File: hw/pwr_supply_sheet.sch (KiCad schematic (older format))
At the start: 16 parts

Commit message: creating hw 3.0.0
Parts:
- added D205: SCHOTTKY_DIODE_V40PW10C, usevolt:SlimDPAK, symbol SCHOTTKY_DIODE_V40PW10C
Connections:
- net VDD: now also D205.3 (CATHODE); no longer D202.P$1 (P)
- new net VIN: D202.P$1 (P), D205.1 (A1), D205.2 (A2)
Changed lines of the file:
@@
 $Descr A4 11693 8268
 encoding utf-8
-Sheet 2 11
+Sheet 2 12
 Title "Power supply"
 Date "2016-08-20"
@@
 Comment4 ""
 $EndDescr
-Text HLabel 1350 3850 0    60   Input ~ 0
+Text HLabel 900  3850 0    60   Input ~ 0
 VIN
 $Comp
@@
 	6850 3600 6850 3850
 $Comp
-L +5V #PWR06
+L +5V #PWR207
 U 1 1 57B831F8
 P 6850 3600
-F 0 "#PWR06" H 6850 3450 50  0001 C CNN
+F 0 "#PWR207" H 6850 3450 50  0001 C CNN
 F 1 "+5V" H 6865 3773 50  0000 C CNN
 F 2 "" H 6850 3600 50  0000 C CNN
@@
 Connection ~ 6850 3750
 $Comp
-L +3V3 #PWR07
+L +3V3 #PWR208
 U 1 1 57B83259
 P 8600 3600
-F 0 "#PWR07" H 8600 3450 50  0001 C CNN
+F 0 "#PWR208" H 8600 3450 50  0001 C CNN
 F 1 "+3V3" H 8615 3773 50  0000 C CNN
 F 2 "" H 8600 3600 50  0000 C CNN
@@
 $EndComp
 Wire Wire Line
-	1350 3850 1700 3850
+	900  3850 1700 3850
 Wire Wire Line
 	3800 3700 4550 3700
@@
 Wire Wire Line
 	8750 3600 8600 3600
-Text HLabel 1350 3450 0    60   Output ~ 0
+Text HLabel 950  5000 0    60   Output ~ 0
 VDD
 Text HLabel 2700 4300 0    60   Input ~ 0
@@
 NoConn ~ 4550 4050
 $Comp
-L VDD #PWR08
+L VDD #PWR205
 U 1 1 57B9C56A
 P 3800 2100
-F 0 "#PWR08" H 3800 1950 50  0001 C CNN
+F 0 "#PWR205" H 3800 1950 50  0001 C CNN
 F 1 "VDD" H 3817 2273 50  0000 C CNN
 F 2 "" H 3800 2100 50  0000 C CNN
@@
 $EndComp
 $Comp
-L PWR_FLAG #FLG09
+L PWR_FLAG #FLG201
 U 1 1 57B9C59C
 P 3800 2300
-F 0 "#FLG09" H 3800 2395 50  0001 C CNN
+F 0 "#FLG201" H 3800 2395 50  0001 C CNN
 F 1 "PWR_FLAG" H 3800 2523 50  0000 C CNN
 F 2 "" H 3800 2300 50  0000 C CNN
@@
 	3800 2300 3800 2100
 $Comp
-L GND #PWR010
+L GND #PWR206
 U 1 1 57B9D351
 P 4300 2350
-F 0 "#PWR010" H 4300 2100 50  0001 C CNN
+F 0 "#PWR206" H 4300 2100 50  0001 C CNN
 F 1 "GND" H 4305 2177 50  0000 C CNN
 F 2 "" H 4300 2350 50  0000 C CNN
@@
 $EndComp
 $Comp
-L PWR_FLAG #FLG011
+L PWR_FLAG #FLG202
 U 1 1 57B9D3A1
 P 4300 2150
-F 0 "#FLG011" H 4300 2245 50  0001 C CNN
+F 0 "#FLG202" H 4300 2245 50  0001 C CNN
 F 1 "PWR_FLAG" H 4300 2374 50  0000 C CNN
 F 2 "" H 4300 2150 50  0000 C CNN
@@
 	4300 2150 4300 2350
 $Comp
-L GND #PWR012
+L GND #PWR204
 U 1 1 57CF1F5E
 P 2800 4500
-F 0 "#PWR012" H 2800 4250 50  0001 C CNN
+F 0 "#PWR204" H 2800 4250 50  0001 C CNN
 F 1 "GND" H 2805 4327 50  0000 C CNN
 F 2 "" H 2800 4500 50  0000 C CNN
@@
 	3800 3850 3800 3700
 Wire Wire Line
-	1350 3450 1500 3450
-Wire Wire Line
-	1500 3450 1500 3850
+	950  5000 1150 5000
 Connection ~ 1500 3850
 Wire Wire Line
@@
 VBAT
 $Comp
-L +BATT #PWR013
+L +BATT #PWR202
 U 1 1 5988E784
 P 2400 1950
-F 0 "#PWR013" H 2400 1800 50  0001 C CNN
+F 0 "#PWR202" H 2400 1800 50  0001 C CNN
 F 1 "+BATT" H 2415 2123 50  0000 C CNN
 F 2 "" H 2400 1950 50  0000 C CNN
@@
 Connection ~ 1550 2700
 $Comp
-L GND #PWR014
+L GND #PWR201
 U 1 1 5988FF98
 P 1550 3150
-F 0 "#PWR014" H 1550 2900 50  0001 C CNN
+F 0 "#PWR201" H 1550 2900 50  0001 C CNN
 F 1 "GND" H 1555 2977 50  0000 C CNN
 F 2 "" H 1550 3150 50  0000 C CNN
@@
 $EndComp
 $Comp
-L GND #PWR015
+L GND #PWR203
 U 1 1 598C262D
 P 2400 2950
-F 0 "#PWR015" H 2400 2700 50  0001 C CNN
+F 0 "#PWR203" H 2400 2700 50  0001 C CNN
 F 1 "GND" H 2405 2777 50  0000 C CNN
 F 2 "" H 2400 2950 50  0000 C CNN
@@
 	2400 2950 2400 2850
 Wire Wire Line
-	2400 2550 2400 2450
+	2400 2450 2400 2550
 Connection ~ 2400 2050
 Wire Wire Line
@@
 Text HLabel 2800 2500 2    60   Output ~ 0
 VBAT_SENSE
+$Comp
+L SCHOTTKY_DIODE_V40PW10C D205
+U 1 1 59C29BB6
+P 1550 5050
+F 0 "D205" H 1550 5397 60  0000 C CNN
+F 1 "SCHOTTKY_DIODE_V40PW10C" H 1550 5291 60  0000 C CNN
+F 2 "usevolt:SlimDPAK" H 1350 4700 60  0001 C CNN
+F 3 "http://www.farnell.com/datasheets/2245239.pdf?_ga=2.16591231.874534928.1505194133-1862443086.1504075057" H 1350 4700 60  0001 C CNN
+F 4 "2535169" H 1900 5650 60  0001 C CNN "1st Source Part Number"
+F 5 "Digikey" H 2000 5750 60  0001 C CNN "2nd Source"
+F 6 "Farnell" H 1800 5550 60  0001 C CNN "1st Source"
+F 7 "V40PW10CHM3/I" H 1700 5450 60  0001 C CNN "Manufacturer Part Number"
+F 8 "V40PW10CHM3/IGICT-ND" H 2100 5850 60  0001 C CNN "2nd Source Part Number"
+F 9 "VISHAY" H 1600 5350 60  0001 C CNN "Manufacturer"
+	1    1550 5050
+	-1   0    0    -1
+$EndComp
+Wire Wire Line
+	1950 5050 2250 5050
+Wire Wire Line
+	2250 5050 2250 4350
+Wire Wire Line
+	2250 4350 1500 4350
+Wire Wire Line
+	1500 4350 1500 3850
+Wire Wire Line
+	1950 4950 2100 4950
+Wire Wire Line
+	2100 4950 2100 5050
+Connection ~ 2100 5050
 $EndSCHEMATC

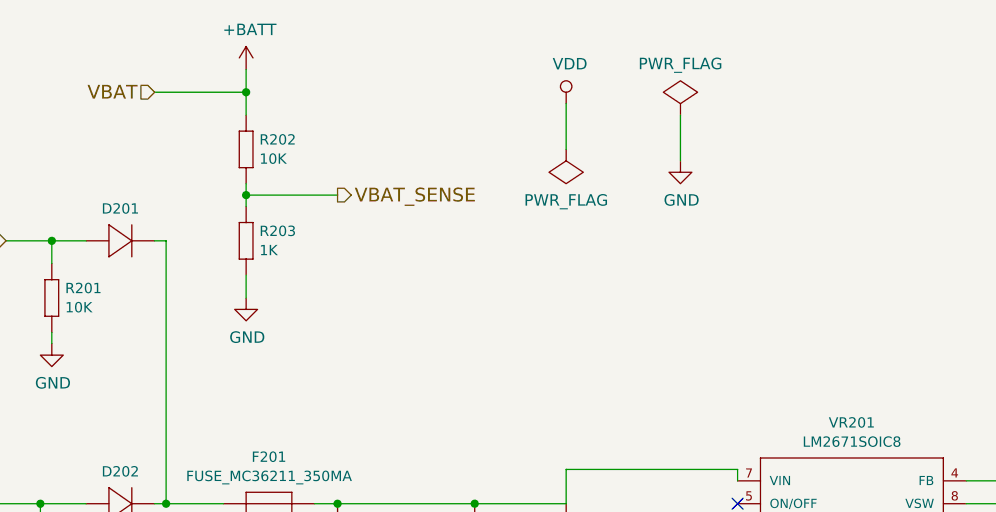
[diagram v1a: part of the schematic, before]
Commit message: key_50 moved out from ISP pin
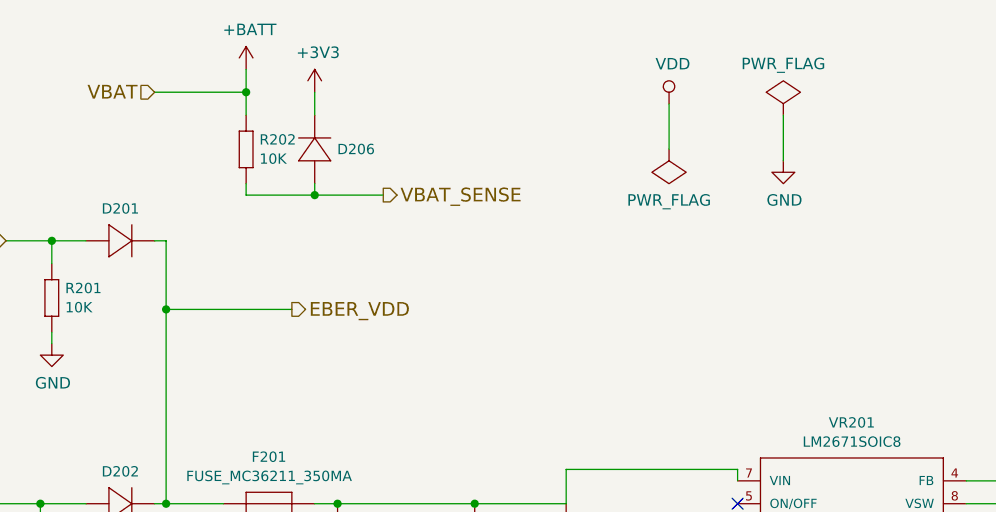
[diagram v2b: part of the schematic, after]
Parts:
- removed R203: 1K, multicomp:0603, symbol 1K
- added D206: DIODE_RS07J-GS18, usevolt:DO219AB, symbol DIODE_RS07J-GS18
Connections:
- net +3V3: now also D206.P$2 (N)
- net VBAT_SENSE: now also D206.P$1 (P)
- net EBER_VDD: now reaches D201.P$2 (N), D202.P$2 (N), F201.P$1
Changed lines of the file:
@@
 	6850 3600 6850 3850
 $Comp
-L +5V #PWR207
+L +5V #PWR06
 U 1 1 57B831F8
 P 6850 3600
-F 0 "#PWR207" H 6850 3450 50  0001 C CNN
+F 0 "#PWR06" H 6850 3450 50  0001 C CNN
 F 1 "+5V" H 6865 3773 50  0000 C CNN
 F 2 "" H 6850 3600 50  0000 C CNN
@@
 Connection ~ 6850 3750
 $Comp
-L +3V3 #PWR208
+L +3V3 #PWR07
 U 1 1 57B83259
 P 8600 3600
-F 0 "#PWR208" H 8600 3450 50  0001 C CNN
+F 0 "#PWR07" H 8600 3450 50  0001 C CNN
 F 1 "+3V3" H 8615 3773 50  0000 C CNN
 F 2 "" H 8600 3600 50  0000 C CNN
@@
 NoConn ~ 4550 4050
 $Comp
-L VDD #PWR205
+L VDD #PWR08
 U 1 1 57B9C56A
-P 3800 2100
-F 0 "#PWR205" H 3800 1950 50  0001 C CNN
-F 1 "VDD" H 3817 2273 50  0000 C CNN
-F 2 "" H 3800 2100 50  0000 C CNN
-F 3 "" H 3800 2100 50  0000 C CNN
-	1    3800 2100
-	1    0    0    -1
-$EndComp
-$Comp
-L PWR_FLAG #FLG201
+P 4250 2100
+F 0 "#PWR08" H 4250 1950 50  0001 C CNN
+F 1 "VDD" H 4267 2273 50  0000 C CNN
+F 2 "" H 4250 2100 50  0000 C CNN
+F 3 "" H 4250 2100 50  0000 C CNN
+	1    4250 2100
+	1    0    0    -1
+$EndComp
+$Comp
+L PWR_FLAG #FLG09
 U 1 1 57B9C59C
-P 3800 2300
-F 0 "#FLG201" H 3800 2395 50  0001 C CNN
-F 1 "PWR_FLAG" H 3800 2523 50  0000 C CNN
-F 2 "" H 3800 2300 50  0000 C CNN
-F 3 "" H 3800 2300 50  0000 C CNN
-	1    3800 2300
+P 4250 2300
+F 0 "#FLG09" H 4250 2395 50  0001 C CNN
+F 1 "PWR_FLAG" H 4250 2523 50  0000 C CNN
+F 2 "" H 4250 2300 50  0000 C CNN
+F 3 "" H 4250 2300 50  0000 C CNN
+	1    4250 2300
 	-1   0    0    1
 $EndComp
 Wire Wire Line
-	3800 2300 3800 2100
-$Comp
-L GND #PWR206
+	4250 2300 4250 2100
+$Comp
+L GND #PWR010
 U 1 1 57B9D351
-P 4300 2350
-F 0 "#PWR206" H 4300 2100 50  0001 C CNN
-F 1 "GND" H 4305 2177 50  0000 C CNN
-F 2 "" H 4300 2350 50  0000 C CNN
-F 3 "" H 4300 2350 50  0000 C CNN
-	1    4300 2350
-	1    0    0    -1
-$EndComp
-$Comp
-L PWR_FLAG #FLG202
+P 4750 2350
+F 0 "#PWR010" H 4750 2100 50  0001 C CNN
+F 1 "GND" H 4755 2177 50  0000 C CNN
+F 2 "" H 4750 2350 50  0000 C CNN
+F 3 "" H 4750 2350 50  0000 C CNN
+	1    4750 2350
+	1    0    0    -1
+$EndComp
+$Comp
+L PWR_FLAG #FLG011
 U 1 1 57B9D3A1
-P 4300 2150
-F 0 "#FLG202" H 4300 2245 50  0001 C CNN
-F 1 "PWR_FLAG" H 4300 2374 50  0000 C CNN
-F 2 "" H 4300 2150 50  0000 C CNN
-F 3 "" H 4300 2150 50  0000 C CNN
-	1    4300 2150
-	1    0    0    -1
-$EndComp
-Wire Wire Line
-	4300 2150 4300 2350
-$Comp
-L GND #PWR204
+P 4750 2150
+F 0 "#FLG011" H 4750 2245 50  0001 C CNN
+F 1 "PWR_FLAG" H 4750 2374 50  0000 C CNN
+F 2 "" H 4750 2150 50  0000 C CNN
+F 3 "" H 4750 2150 50  0000 C CNN
+	1    4750 2150
+	1    0    0    -1
+$EndComp
+Wire Wire Line
+	4750 2150 4750 2350
+$Comp
+L GND #PWR012
 U 1 1 57CF1F5E
 P 2800 4500
-F 0 "#PWR204" H 2800 4250 50  0001 C CNN
+F 0 "#PWR012" H 2800 4250 50  0001 C CNN
 F 1 "GND" H 2805 4327 50  0000 C CNN
 F 2 "" H 2800 4500 50  0000 C CNN
@@
 VBAT
 $Comp
-L +BATT #PWR202
+L +BATT #PWR013
 U 1 1 5988E784
 P 2400 1950
-F 0 "#PWR202" H 2400 1800 50  0001 C CNN
+F 0 "#PWR013" H 2400 1800 50  0001 C CNN
 F 1 "+BATT" H 2415 2123 50  0000 C CNN
 F 2 "" H 2400 1950 50  0000 C CNN
@@
 Connection ~ 1550 2700
 $Comp
-L GND #PWR201
+L GND #PWR014
 U 1 1 5988FF98
 P 1550 3150
-F 0 "#PWR201" H 1550 2900 50  0001 C CNN
+F 0 "#PWR014" H 1550 2900 50  0001 C CNN
 F 1 "GND" H 1555 2977 50  0000 C CNN
 F 2 "" H 1550 3150 50  0000 C CNN
@@
 	0    1    1    0
 $EndComp
-$Comp
-L 1K R203
-U 1 1 598C25B6
-P 2400 2650
-F 0 "R203" V 2408 2708 45  0000 L CNN
-F 1 "1K" V 2492 2708 45  0000 L CNN
-F 2 "multicomp:0603" H 2430 2800 20  0001 C CNN
-F 3 "" H 2369 2689 60  0001 C CNN
-F 4 "9330380" H 2769 3089 60  0001 C CNN "1st Source Part Number"
-F 5 "Farnell" H 2669 2989 60  0001 C CNN "1st Source"
-F 6 "MC0063W060311K" H 2569 2889 60  0001 C CNN "Manufacturer Part Number"
-F 7 "MULTICOMP" H 2469 2789 60  0001 C CNN "Manufacturer"
-	1    2400 2650
-	0    1    1    0
-$EndComp
-$Comp
-L GND #PWR203
-U 1 1 598C262D
-P 2400 2950
-F 0 "#PWR203" H 2400 2700 50  0001 C CNN
-F 1 "GND" H 2405 2777 50  0000 C CNN
-F 2 "" H 2400 2950 50  0000 C CNN
-F 3 "" H 2400 2950 50  0000 C CNN
-	1    2400 2950
-	1    0    0    -1
-$EndComp
-Wire Wire Line
-	2400 2950 2400 2850
-Wire Wire Line
-	2400 2450 2400 2550
 Connection ~ 2400 2050
 Wire Wire Line
-	2400 2500 2800 2500
-Connection ~ 2400 2500
-Text HLabel 2800 2500 2    60   Output ~ 0
+	2400 2500 3000 2500
+Text HLabel 3000 2500 2    60   Output ~ 0
 VBAT_SENSE
 $Comp
@@
 	2100 4950 2100 5050
 Connection ~ 2100 5050
+Wire Wire Line
+	2400 2500 2400 2450
+$Comp
+L DIODE_RS07J-GS18 D206
+U 1 1 59C24380
+P 2700 2250
+F 0 "D206" V 2650 2152 45  0000 R CNN
+F 1 "DIODE_RS07J-GS18" H 2720 2190 45  0001 L BNN
+F 2 "usevolt:DO219AB" H 2730 2400 20  0001 C CNN
+F 3 "http://www.vishay.com/docs/85742/rs07b.pdf" H 2720 2270 60  0001 C CNN
+F 4 "1864882" H 3320 2870 60  0001 C CNN "2nd Source Part Number"
+F 5 "Digi-Key" H 3020 2570 60  0001 C CNN "1st Source"
+F 6 "Farnell" H 3220 2770 60  0001 C CNN "2nd Source"
+F 7 "RS07J-GS18" H 2920 2470 60  0001 C CNN "Manufacturer Part Number"
+F 8 "RS07J-GS18-ND" H 3120 2670 60  0001 C CNN "1st Source Part Number"
+F 9 "Vishay Semiconductor Diodes Division" H 2820 2370 60  0001 C CNN "Manufacturer"
+	1    2700 2250
+	0    -1   -1   0
+$EndComp
+$Comp
+L +3V3 #PWR015
+U 1 1 59C244E7
+P 2700 2050
+F 0 "#PWR015" H 2700 1900 50  0001 C CNN
+F 1 "+3V3" H 2715 2223 50  0000 C CNN
+F 2 "" H 2700 2050 50  0000 C CNN
+F 3 "" H 2700 2050 50  0000 C CNN
+	1    2700 2050
+	1    0    0    -1
+$EndComp
+Wire Wire Line
+	2700 2150 2700 2050
+Wire Wire Line
+	2700 2450 2700 2500
+Connection ~ 2700 2500
+Text HLabel 2600 3000 2    60   Output ~ 0
+EBER_VDD
+Wire Wire Line
+	2050 3000 2600 3000
+Connection ~ 2050 3000
 $EndSCHEMATC

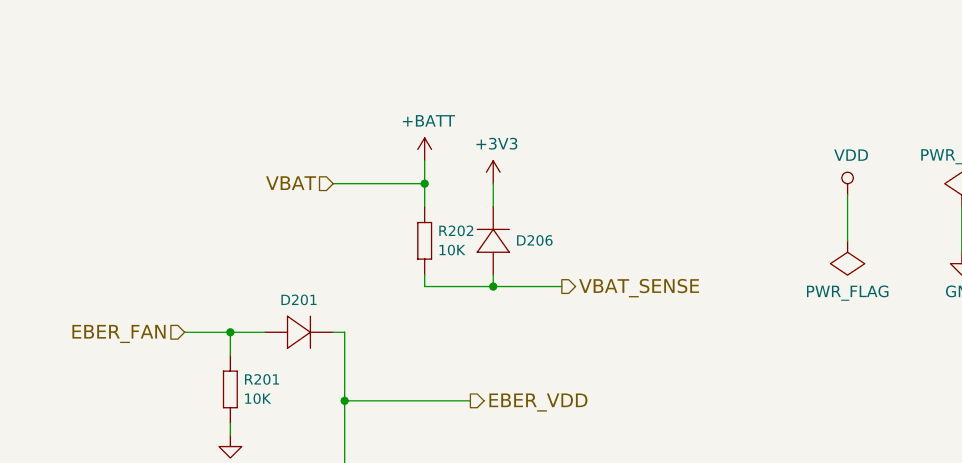
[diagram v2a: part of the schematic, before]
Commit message: radio & aux are on when ign key is on
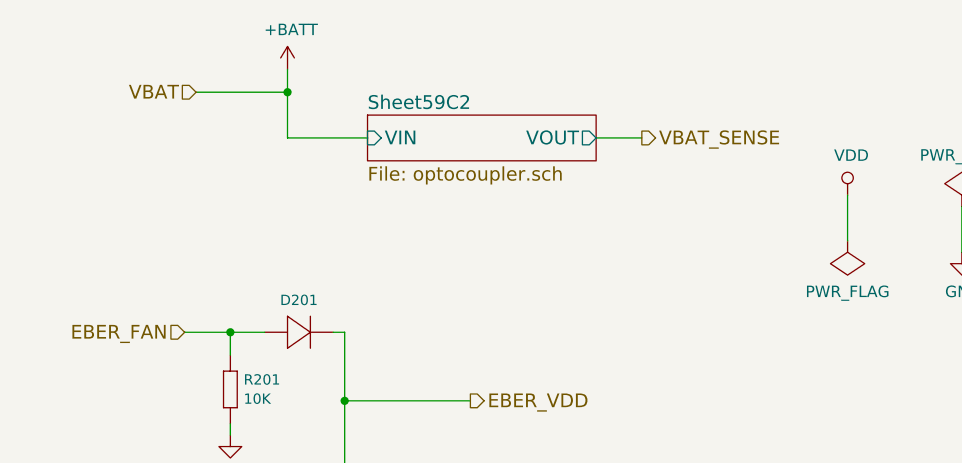
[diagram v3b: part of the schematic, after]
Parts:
- removed D206: DIODE_RS07J-GS18, usevolt:DO219AB, symbol DIODE_RS07J-GS18
- removed R202: 10K, multicomp:0603, symbol 10K
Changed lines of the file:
@@
 EESchema Schematic File Version 2
 LIBS:kemet
-LIBS:multicomp
 LIBS:power
 LIBS:usevolt
 LIBS:wurth_elektronik_LED
+LIBS:yageo
 LIBS:fsb-cache
 EELAYER 26 0
@@
 $Descr A4 11693 8268
 encoding utf-8
-Sheet 2 12
+Sheet 2 9
 Title "Power supply"
 Date "2016-08-20"
@@
 	6850 3600 6850 3850
 $Comp
-L +5V #PWR06
+L +5V #PWR07
 U 1 1 57B831F8
 P 6850 3600
-F 0 "#PWR06" H 6850 3450 50  0001 C CNN
+F 0 "#PWR07" H 6850 3450 50  0001 C CNN
 F 1 "+5V" H 6865 3773 50  0000 C CNN
 F 2 "" H 6850 3600 50  0000 C CNN
@@
 Connection ~ 6850 3750
 $Comp
-L +3V3 #PWR07
+L +3V3 #PWR08
 U 1 1 57B83259
 P 8600 3600
-F 0 "#PWR07" H 8600 3450 50  0001 C CNN
+F 0 "#PWR08" H 8600 3450 50  0001 C CNN
 F 1 "+3V3" H 8615 3773 50  0000 C CNN
 F 2 "" H 8600 3600 50  0000 C CNN
@@
 NoConn ~ 4550 4050
 $Comp
-L VDD #PWR08
+L VDD #PWR09
 U 1 1 57B9C56A
 P 4250 2100
-F 0 "#PWR08" H 4250 1950 50  0001 C CNN
+F 0 "#PWR09" H 4250 1950 50  0001 C CNN
 F 1 "VDD" H 4267 2273 50  0000 C CNN
 F 2 "" H 4250 2100 50  0000 C CNN
@@
 $EndComp
 $Comp
-L PWR_FLAG #FLG09
+L PWR_FLAG #FLG010
 U 1 1 57B9C59C
 P 4250 2300
-F 0 "#FLG09" H 4250 2395 50  0001 C CNN
+F 0 "#FLG010" H 4250 2395 50  0001 C CNN
 F 1 "PWR_FLAG" H 4250 2523 50  0000 C CNN
 F 2 "" H 4250 2300 50  0000 C CNN
@@
 	4250 2300 4250 2100
 $Comp
-L GND #PWR010
+L GND #PWR011
 U 1 1 57B9D351
 P 4750 2350
-F 0 "#PWR010" H 4750 2100 50  0001 C CNN
+F 0 "#PWR011" H 4750 2100 50  0001 C CNN
 F 1 "GND" H 4755 2177 50  0000 C CNN
 F 2 "" H 4750 2350 50  0000 C CNN
@@
 $EndComp
 $Comp
-L PWR_FLAG #FLG011
+L PWR_FLAG #FLG012
 U 1 1 57B9D3A1
 P 4750 2150
-F 0 "#FLG011" H 4750 2245 50  0001 C CNN
+F 0 "#FLG012" H 4750 2245 50  0001 C CNN
 F 1 "PWR_FLAG" H 4750 2374 50  0000 C CNN
 F 2 "" H 4750 2150 50  0000 C CNN
@@
 	4750 2150 4750 2350
 $Comp
-L GND #PWR012
+L GND #PWR013
 U 1 1 57CF1F5E
 P 2800 4500
-F 0 "#PWR012" H 2800 4250 50  0001 C CNN
+F 0 "#PWR013" H 2800 4250 50  0001 C CNN
 F 1 "GND" H 2805 4327 50  0000 C CNN
 F 2 "" H 2800 4500 50  0000 C CNN
@@
 	1    0    0    -1
 $EndComp
-Text HLabel 2000 2050 0    60   Input ~ 0
+Text HLabel 1400 1650 0    60   Input ~ 0
 VBAT
 $Comp
-L +BATT #PWR013
+L +BATT #PWR014
 U 1 1 5988E784
-P 2400 1950
-F 0 "#PWR013" H 2400 1800 50  0001 C CNN
-F 1 "+BATT" H 2415 2123 50  0000 C CNN
-F 2 "" H 2400 1950 50  0000 C CNN
-F 3 "" H 2400 1950 50  0000 C CNN
-	1    2400 1950
-	1    0    0    -1
-$EndComp
-Wire Wire Line
-	2400 1950 2400 2150
-Wire Wire Line
-	2400 2050 2000 2050
+P 1800 1550
+F 0 "#PWR014" H 1800 1400 50  0001 C CNN
+F 1 "+BATT" H 1815 1723 50  0000 C CNN
+F 2 "" H 1800 1550 50  0000 C CNN
+F 3 "" H 1800 1550 50  0000 C CNN
+	1    1800 1550
+	1    0    0    -1
+$EndComp
+Wire Wire Line
+	1800 1550 1800 1850
+Wire Wire Line
+	1800 1650 1400 1650
 Text HLabel 1350 2700 0    60   Input ~ 0
 EBER_FAN
@@
 Connection ~ 1550 2700
 $Comp
-L GND #PWR014
+L GND #PWR015
 U 1 1 5988FF98
 P 1550 3150
-F 0 "#PWR014" H 1550 2900 50  0001 C CNN
+F 0 "#PWR015" H 1550 2900 50  0001 C CNN
 F 1 "GND" H 1555 2977 50  0000 C CNN
 F 2 "" H 1550 3150 50  0000 C CNN
@@
 Wire Wire Line
 	1550 2700 1550 2800
-$Comp
-L 10K R202
-U 1 1 598C2542
-P 2400 2250
-F 0 "R202" V 2408 2308 45  0000 L CNN
-F 1 "10K" V 2492 2308 45  0000 L CNN
-F 2 "multicomp:0603" H 2430 2400 20  0001 C CNN
-F 3 "http://www.farnell.com/datasheets/1788326.pdf?_ga=1.214208087.1948984246.1460023966" H 2369 2289 60  0001 C CNN
-F 4 "9330399" H 2769 2689 60  0001 C CNN "1st Source Part Number"
-F 5 "Farnell" H 2669 2589 60  0001 C CNN "1st Source"
-F 6 "MC0063W0603110K" H 2569 2489 60  0001 C CNN "Manufacturer Part Number"
-F 7 "MULTICOMP" H 2469 2389 60  0001 C CNN "Manufacturer"
-	1    2400 2250
-	0    1    1    0
-$EndComp
-Connection ~ 2400 2050
-Wire Wire Line
-	2400 2500 3000 2500
-Text HLabel 3000 2500 2    60   Output ~ 0
+Connection ~ 1800 1650
+Text HLabel 3350 1850 2    60   Output ~ 0
 VBAT_SENSE
 $Comp
@@
 	2100 4950 2100 5050
 Connection ~ 2100 5050
-Wire Wire Line
-	2400 2500 2400 2450
-$Comp
-L DIODE_RS07J-GS18 D206
-U 1 1 59C24380
-P 2700 2250
-F 0 "D206" V 2650 2152 45  0000 R CNN
-F 1 "DIODE_RS07J-GS18" H 2720 2190 45  0001 L BNN
-F 2 "usevolt:DO219AB" H 2730 2400 20  0001 C CNN
-F 3 "http://www.vishay.com/docs/85742/rs07b.pdf" H 2720 2270 60  0001 C CNN
-F 4 "1864882" H 3320 2870 60  0001 C CNN "2nd Source Part Number"
-F 5 "Digi-Key" H 3020 2570 60  0001 C CNN "1st Source"
-F 6 "Farnell" H 3220 2770 60  0001 C CNN "2nd Source"
-F 7 "RS07J-GS18" H 2920 2470 60  0001 C CNN "Manufacturer Part Number"
-F 8 "RS07J-GS18-ND" H 3120 2670 60  0001 C CNN "1st Source Part Number"
-F 9 "Vishay Semiconductor Diodes Division" H 2820 2370 60  0001 C CNN "Manufacturer"
-	1    2700 2250
-	0    -1   -1   0
-$EndComp
-$Comp
-L +3V3 #PWR015
-U 1 1 59C244E7
-P 2700 2050
-F 0 "#PWR015" H 2700 1900 50  0001 C CNN
-F 1 "+3V3" H 2715 2223 50  0000 C CNN
-F 2 "" H 2700 2050 50  0000 C CNN
-F 3 "" H 2700 2050 50  0000 C CNN
-	1    2700 2050
-	1    0    0    -1
-$EndComp
-Wire Wire Line
-	2700 2150 2700 2050
-Wire Wire Line
-	2700 2450 2700 2500
-Connection ~ 2700 2500
 Text HLabel 2600 3000 2    60   Output ~ 0
 EBER_VDD
@@
 	2050 3000 2600 3000
 Connection ~ 2050 3000
+$Sheet
+S 2150 1750 1000 200
+U 59C2BC93
+F0 "Sheet59C2" 60
+F1 "optocoupler.sch" 60
+F2 "VOUT" O R 3150 1850 60
+F3 "VIN" I L 2150 1850 60
+$EndSheet
+Wire Wire Line
+	1800 1850 2150 1850
+Wire Wire Line
+	3150 1850 3350 1850
 $EndSCHEMATC
